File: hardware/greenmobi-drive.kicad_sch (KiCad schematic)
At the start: 32 parts, among them J1 GND, J2 Sensors, J3 UBAT, J4 USB_C_Receptacle_USB2.0_14P, J5 CAN, U1 BMI323, U2 TJA1051T-3

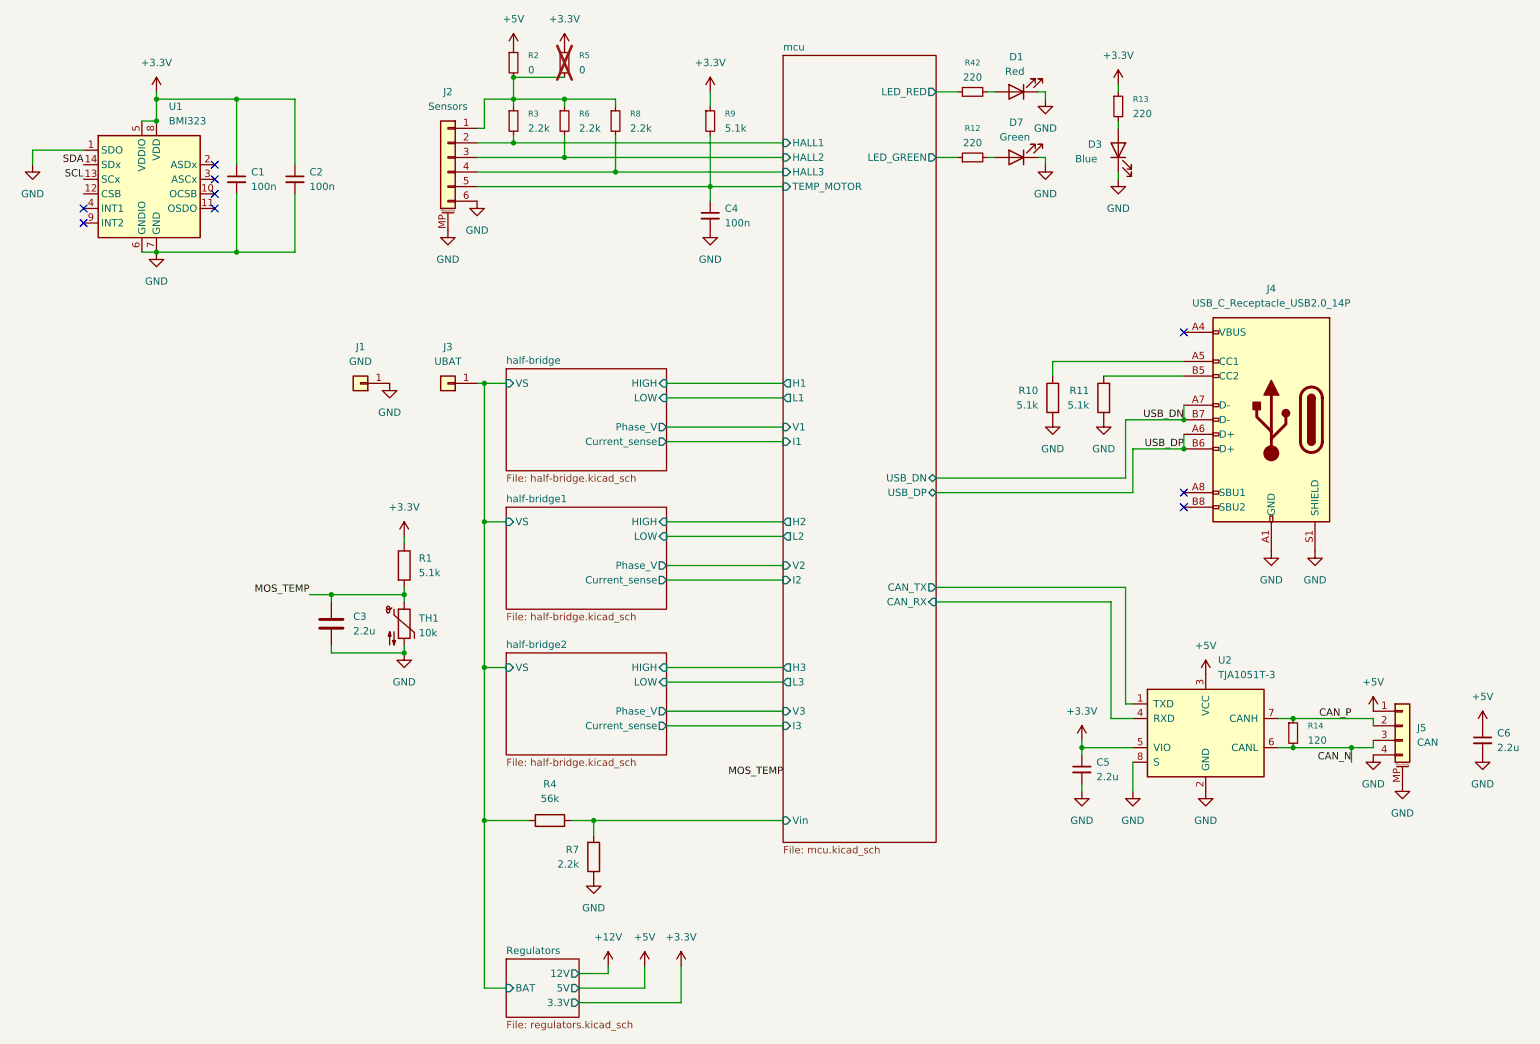
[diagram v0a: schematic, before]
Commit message: Mounting holes alignment
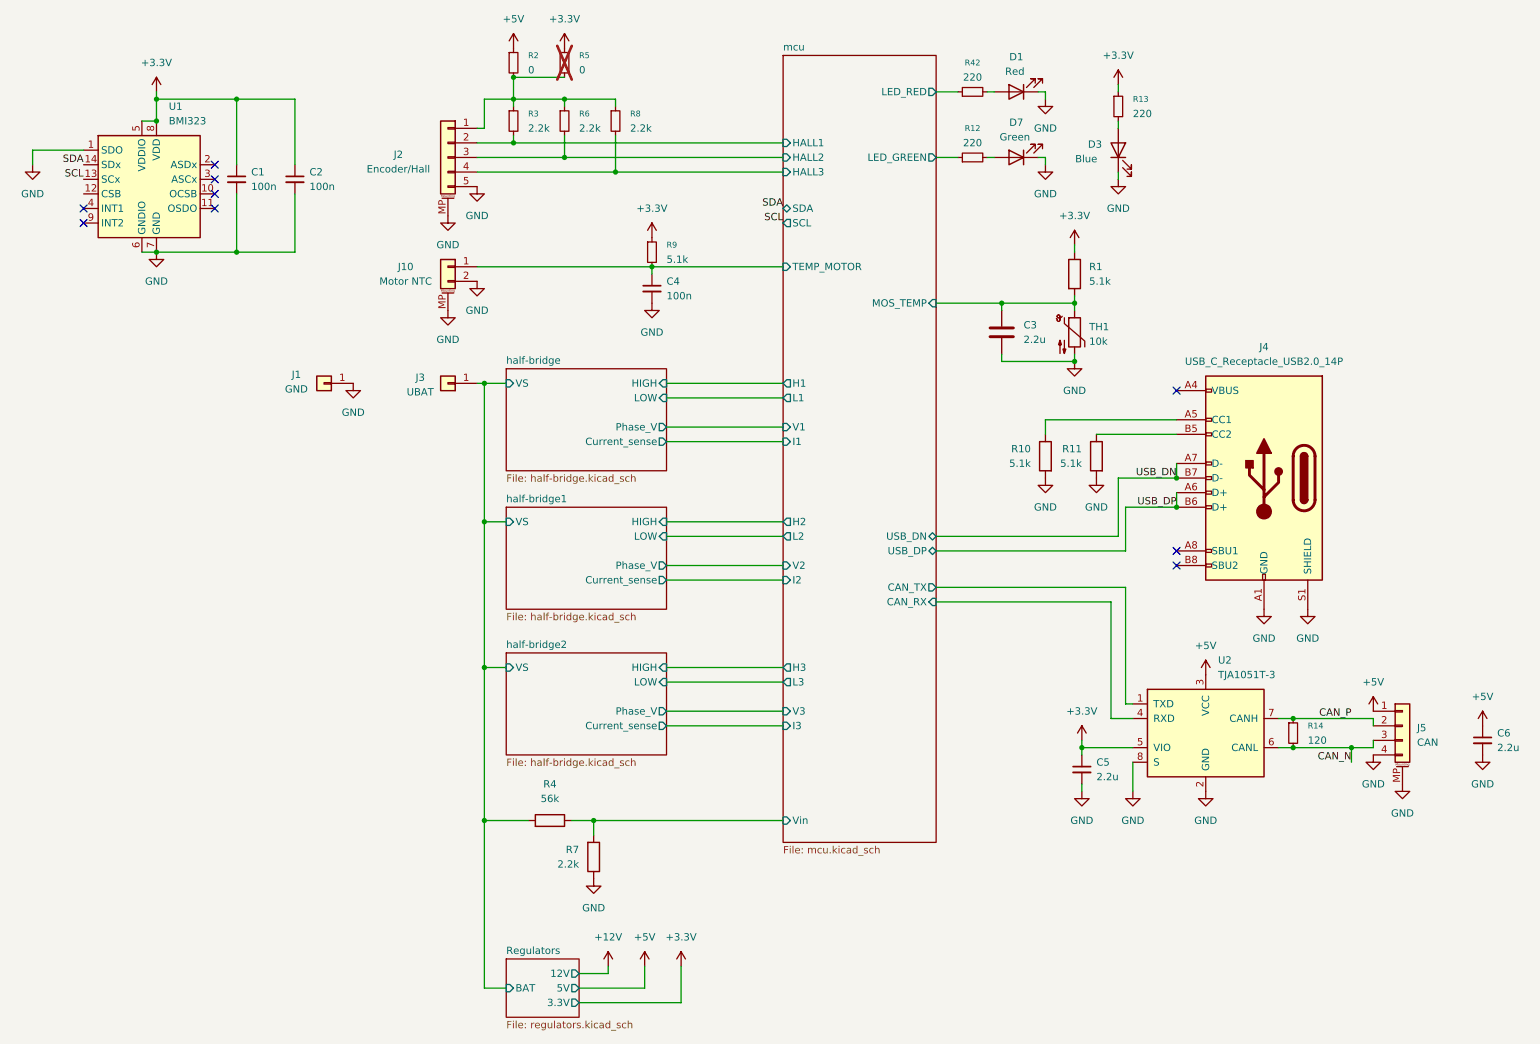
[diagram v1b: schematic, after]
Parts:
- added J10: Motor NTC, Connector_JST:JST_GH_SM02B-GHS-TB_1x02-1MP_P1.25mm_Horizontal, symbol Connector_Generic_MountingPin:Conn_01x02_MountingPin
- J2: value Sensors -> Encoder/Hall; footprint Connector_JST:JST_GH_SM06B-GHS-TB_1x06-1MP_P1.25mm_Horizontal -> Connector_JST:JST_GH_SM05B-GHS-TB_1x05-1MP_P1.25mm_Horizontal; symbol Connector_Generic_MountingPin:Conn_01x06_MountingPin -> Connector_Generic_MountingPin:Conn_01x05_MountingPin
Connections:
- net GND: now also J2.5 (Pin_5), J10.2 (Pin_2), J10.MP (MountPin); no longer J2.6 (Pin_6)
- net mcu/TEMP_MOTOR: now also J10.1 (Pin_1); no longer J2.5 (Pin_5)
- net MOS_TEMP renamed mcu/MOS_TEMP
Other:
- sheet mcu ports: added MOS_TEMP, SCL, SDA; removed none
- moved on the sheet: C3, C4, J1, J4, R1, R10, R11, R9, TH1

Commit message: Capacitors sourced
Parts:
- C1, C2, C4: LCSC (none) -> C77020
- C3, C5, C6: LCSC (none) -> C170151
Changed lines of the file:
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@@
 			)
 		)
-		(property "Sim.Type" ""
-			(at 200.66 69.85 0)
-			(effects
-				(font
-					(size 1.27 1.27)
-				)
-				(hide yes)
-			)
-		)
 		(pin "1"
 		)
@@
 			)
 		)
-		(property "Sim.Type" ""
-			(at 120.65 33.02 0)
-			(effects
-				(font
-					(size 1.27 1.27)
-				)
-				(hide yes)
-			)
-		)
 		(pin "2"
 		)
@@
 			)
 		)
-		(property "Sim.Pins" "1=K 2=A"
-			(at 190.5 39.37 0)
-			(effects
-				(font
-					(size 1.27 1.27)
-				)
-				(hide yes)
-			)
-		)
-		(property "Sim.Type" ""
-			(at 190.5 39.37 0)
-			(effects
-				(font
-					(size 1.27 1.27)
-				)
-				(hide yes)
-			)
-		)
 		(property "LCSC" ""
 			(at 190.5 39.37 90)
@@
 			)
 		)
-		(property "Sim.Type" ""
+		(property "LCSC" "C77020"
 			(at 127 62.23 0)
 			(effects
@@
 			)
 		)
-		(property "Sim.Type" ""
-			(at 111.76 33.02 0)
-			(effects
-				(font
-					(size 1.27 1.27)
-				)
-				(hide yes)
-			)
-		)
 		(pin "2"
 		)
@@
 			)
 		)
-		(property "Sim.Type" ""
+		(property "LCSC" "C170151"
 			(at 201.93 146.05 0)
 			(effects
@@
 			)
 		)
-		(property "Sim.Type" ""
+		(property "LCSC" "C170151"
 			(at 187.96 69.85 0)
 			(effects
@@
 			)
 		)
-		(property "Sim.Type" ""
-			(at 195.58 91.44 0)
-			(effects
-				(font
-					(size 1.27 1.27)
-				)
-				(hide yes)
-			)
-		)
 		(pin "1"
 		)
@@
 			)
 		)
-		(property "Sim.Type" ""
-			(at 69.85 78.74 0)
-			(effects
-				(font
-					(size 1.27 1.27)
-				)
-				(hide yes)
-			)
-		)
 		(pin "1"
 		)
@@
 			)
 		)
-		(property "Sim.Type" ""
-			(at 102.87 22.86 0)
-			(effects
-				(font
-					(size 1.27 1.27)
-				)
-				(hide yes)
-			)
-		)
 		(pin "1"
 		)
@@
 			)
 		)
-		(property "Sim.Type" ""
-			(at 204.47 91.44 0)
-			(effects
-				(font
-					(size 1.27 1.27)
-				)
-				(hide yes)
-			)
-		)
 		(pin "1"
 		)
@@
 			)
 		)
-		(property "Sim.Type" ""
-			(at 238.76 139.7 0)
-			(effects
-				(font
-					(size 1.27 1.27)
-				)
-				(hide yes)
-			)
-		)
 		(pin "2"
 		)
@@
 			)
 		)
+		(property "LCSC" "C77020"
+			(at 54.61 43.18 0)
+			(effects
+				(font
+					(size 1.27 1.27)
+				)
+				(hide yes)
+			)
+		)
 		(pin "2"
 		)
@@
 			)
 		)
-		(property "Sim.Type" ""
-			(at 91.44 78.74 0)
-			(effects
-				(font
-					(size 1.27 1.27)
-				)
-				(hide yes)
-			)
-		)
 		(pin "1"
 		)
@@
 			)
 		)
-		(property "Sim.Type" ""
-			(at 233.68 95.25 0)
-			(effects
-				(font
-					(size 1.27 1.27)
-				)
-				(hide yes)
-			)
-		)
 		(pin "A7"
 		)
@@
 			)
 		)
-		(property "Sim.Type" ""
-			(at 109.22 154.94 90)
-			(effects
-				(font
-					(size 1.27 1.27)
-				)
-				(hide yes)
-			)
-		)
 		(pin "2"
 		)
@@
 			)
 		)
-		(property "Sim.Type" ""
-			(at 116.84 161.29 0)
-			(effects
-				(font
-					(size 1.27 1.27)
-				)
-				(hide yes)
-			)
-		)
 		(pin "2"
 		)
@@
 			)
 		)
+		(property "LCSC" "C77020"
+			(at 64.77 43.18 0)
+			(effects
+				(font
+					(size 1.27 1.27)
+				)
+				(hide yes)
+			)
+		)
 		(pin "2"
 		)
@@
 			)
 		)
-		(property "Sim.Type" ""
-			(at 111.76 22.86 0)
-			(effects
-				(font
-					(size 1.27 1.27)
-				)
-				(hide yes)
-			)
-		)
 		(pin "1"
 		)
@@
 			)
 		)
-		(property "Sim.Type" ""
-			(at 257.81 138.43 0)
-			(effects
-				(font
-					(size 1.27 1.27)
-				)
-				(hide yes)
-			)
-		)
 		(pin "3"
 		)
@@
 			)
 		)
-		(property "Sim.Type" ""
-			(at 223.52 139.7 0)
-			(effects
-				(font
-					(size 1.27 1.27)
-				)
-				(hide yes)
-			)
-		)
 		(pin "6"
 		)
@@
 			)
 		)
-		(property "Sim.Type" ""
-			(at 127 55.88 0)
-			(effects
-				(font
-					(size 1.27 1.27)
-				)
-				(hide yes)
-			)
-		)
 		(pin "2"
 		)
@@
 			)
 		)
-		(property "Sim.Type" ""
-			(at 200.66 59.69 0)
-			(effects
-				(font
-					(size 1.27 1.27)
-				)
-				(hide yes)
-			)
-		)
 		(pin "1"
 		)
@@
 			)
 		)
-		(property "Sim.Pins" "1=K 2=A"
-			(at 190.5 27.94 0)
-			(effects
-				(font
-					(size 1.27 1.27)
-				)
-				(hide yes)
-			)
-		)
-		(property "Sim.Type" ""
-			(at 190.5 27.94 0)
-			(effects
-				(font
-					(size 1.27 1.27)
-				)
-				(hide yes)
-			)
-		)
 		(property "LCSC" ""
 			(at 190.5 27.94 90)
@@
 			)
 		)
-		(property "Sim.Type" ""
-			(at 91.44 39.37 0)
-			(effects
-				(font
-					(size 1.27 1.27)
-				)
-				(hide yes)
-			)
-		)
 		(pin "3"
 		)
@@
 			)
 		)
-		(property "Sim.Pins" "1=K 2=A"
-			(at 208.28 38.1 0)
-			(effects
-				(font
-					(size 1.27 1.27)
-				)
-				(hide yes)
-			)
-		)
-		(property "Sim.Type" ""
-			(at 208.28 38.1 0)
-			(effects
-				(font
-					(size 1.27 1.27)
-				)
-				(hide yes)
-			)
-		)
 		(property "LCSC" ""
 			(at 208.28 38.1 90)
@@
 			)
 		)
-		(property "Sim.Type" ""
+		(property "LCSC" "C170151"
 			(at 271.78 140.97 0)
 			(effects
@@
 			(at 102.87 33.02 0)
 			(effects
-				(font
-					(size 1.27 1.27)
-				)
-				(hide yes)
-			)
-		)
-		(property "Sim.Type" ""
-			(at 102.87 33.02 0)
-			(effects

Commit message: Sourcing complete
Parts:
- D1: LCSC (none) -> C688884
- D3: LCSC (none) -> C779459
- D7: LCSC (none) -> C688883
- J10: LCSC (none) -> C17700380
- J2: LCSC (none) -> C17700383
- J4: LCSC (none) -> C2765186
- J5: LCSC (none) -> C17700382
- R1, R10, R11, R9: LCSC (none) -> C25905
- R12, R13, R42: LCSC (none) -> C2909336
- R14: LCSC (none) -> C25079
- R2, R5: LCSC (none) -> C106231
- R3, R6, R7, R8: LCSC (none) -> C114762
- R4: LCSC (none) -> C17756
- TH1: LCSC (none) -> C77131
- U2: LCSC (none) -> C38695
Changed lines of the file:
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@@
 			)
 		)
+		(property "LCSC" "C77131"
+			(at 200.66 69.85 0)
+			(effects
+				(font
+					(size 1.27 1.27)
+				)
+				(hide yes)
+			)
+		)
 		(pin "1"
 		)
@@
 			)
 		)
+		(property "LCSC" "C2909336"
+			(at 208.28 30.48 0)
+			(effects
+				(font
+					(size 1.27 1.27)
+				)
+				(hide yes)
+			)
+		)
 		(pin "2"
 		)
@@
 			)
 		)
+		(property "LCSC" "C114762"
+			(at 120.65 33.02 0)
+			(effects
+				(font
+					(size 1.27 1.27)
+				)
+				(hide yes)
+			)
+		)
 		(pin "2"
 		)
@@
 			)
 		)
+		(property "LCSC" "C2909336"
+			(at 182.88 39.37 90)
+			(effects
+				(font
+					(size 1.27 1.27)
+				)
+				(hide yes)
+			)
+		)
 		(pin "2"
 		)
@@
 			)
 		)
-		(property "LCSC" ""
+		(property "LCSC" "C688883"
 			(at 190.5 39.37 90)
 			(effects
@@
 			)
 		)
+		(property "LCSC" "C114762"
+			(at 111.76 33.02 0)
+			(effects
+				(font
+					(size 1.27 1.27)
+				)
+				(hide yes)
+			)
+		)
 		(pin "2"
 		)
@@
 			)
 		)
+		(property "LCSC" "C2909336"
+			(at 182.88 27.94 90)
+			(effects
+				(font
+					(size 1.27 1.27)
+				)
+				(hide yes)
+			)
+		)
 		(pin "2"
 		)
@@
 			)
 		)
+		(property "LCSC" "C25905"
+			(at 195.58 91.44 0)
+			(effects
+				(font
+					(size 1.27 1.27)
+				)
+				(hide yes)
+			)
+		)
 		(pin "1"
 		)
@@
 			)
 		)
+		(property "LCSC" "C106231"
+			(at 102.87 22.86 0)
+			(effects
+				(font
+					(size 1.27 1.27)
+				)
+				(hide yes)
+			)
+		)
 		(pin "1"
 		)
@@
 			)
 		)
+		(property "LCSC" "C25905"
+			(at 204.47 91.44 0)
+			(effects
+				(font
+					(size 1.27 1.27)
+				)
+				(hide yes)
+			)
+		)
 		(pin "1"
 		)
@@
 			)
 		)
+		(property "LCSC" "C25079"
+			(at 238.76 139.7 0)
+			(effects
+				(font
+					(size 1.27 1.27)
+				)
+				(hide yes)
+			)
+		)
 		(pin "2"
 		)
@@
 			)
 		)
+		(property "LCSC" "C17700380"
+			(at 91.44 58.42 0)
+			(effects
+				(font
+					(size 1.27 1.27)
+				)
+				(hide yes)
+			)
+		)
 		(pin "1"
 		)
@@
 			)
 		)
+		(property "LCSC" "C2765186"
+			(at 233.68 95.25 0)
+			(effects
+				(font
+					(size 1.27 1.27)
+				)
+				(hide yes)
+			)
+		)
 		(pin "A7"
 		)
@@
 			)
 		)
+		(property "LCSC" "C17756"
+			(at 109.22 154.94 90)
+			(effects
+				(font
+					(size 1.27 1.27)
+				)
+				(hide yes)
+			)
+		)
 		(pin "2"
 		)
@@
 			)
 		)
+		(property "LCSC" "C114762"
+			(at 116.84 161.29 0)
+			(effects
+				(font
+					(size 1.27 1.27)
+				)
+				(hide yes)
+			)
+		)
 		(pin "2"
 		)
@@
 			)
 		)
+		(property "LCSC" "C106231"
+			(at 111.76 22.86 0)
+			(effects
+				(font
+					(size 1.27 1.27)
+				)
+				(hide yes)
+			)
+		)
 		(pin "1"
 		)
@@
 			)
 		)
+		(property "LCSC" "C17700382"
+			(at 257.81 138.43 0)
+			(effects
+				(font
+					(size 1.27 1.27)
+				)
+				(hide yes)
+			)
+		)
 		(pin "3"
 		)
@@
 			)
 		)
+		(property "LCSC" "C38695"
+			(at 223.52 139.7 0)
+			(effects
+				(font
+					(size 1.27 1.27)
+				)
+				(hide yes)
+			)
+		)
 		(pin "6"
 		)
@@
 			)
 		)
+		(property "LCSC" "C25905"
+			(at 127 55.88 0)
+			(effects
+				(font
+					(size 1.27 1.27)
+				)
+				(hide yes)
+			)
+		)
 		(pin "2"
 		)
@@
 			)
 		)
+		(property "LCSC" "C25905"
+			(at 200.66 59.69 0)
+			(effects
+				(font
+					(size 1.27 1.27)
+				)
+				(hide yes)
+			)
+		)
 		(pin "1"
 		)
@@
 			)
 		)
-		(property "LCSC" ""
+		(property "LCSC" "C688884"
 			(at 190.5 27.94 90)
 			(effects
@@
 			)
 		)
+		(property "LCSC" "C17700383"
+			(at 91.44 39.37 0)
+			(effects
+				(font
+					(size 1.27 1.27)
+				)
+				(hide yes)
+			)
+		)
 		(pin "3"
 		)
@@
 			)
 		)
-		(property "LCSC" ""
+		(property "LCSC" "C779459"
 			(at 208.28 38.1 90)
 			(effects
@@
 			(at 102.87 33.02 0)
 			(effects
+				(font
+					(size 1.27 1.27)
+				)
+				(hide yes)
+			)
+		)
+		(property "LCSC" "C114762"
+			(at 102.87 33.02 0)
+			(effects

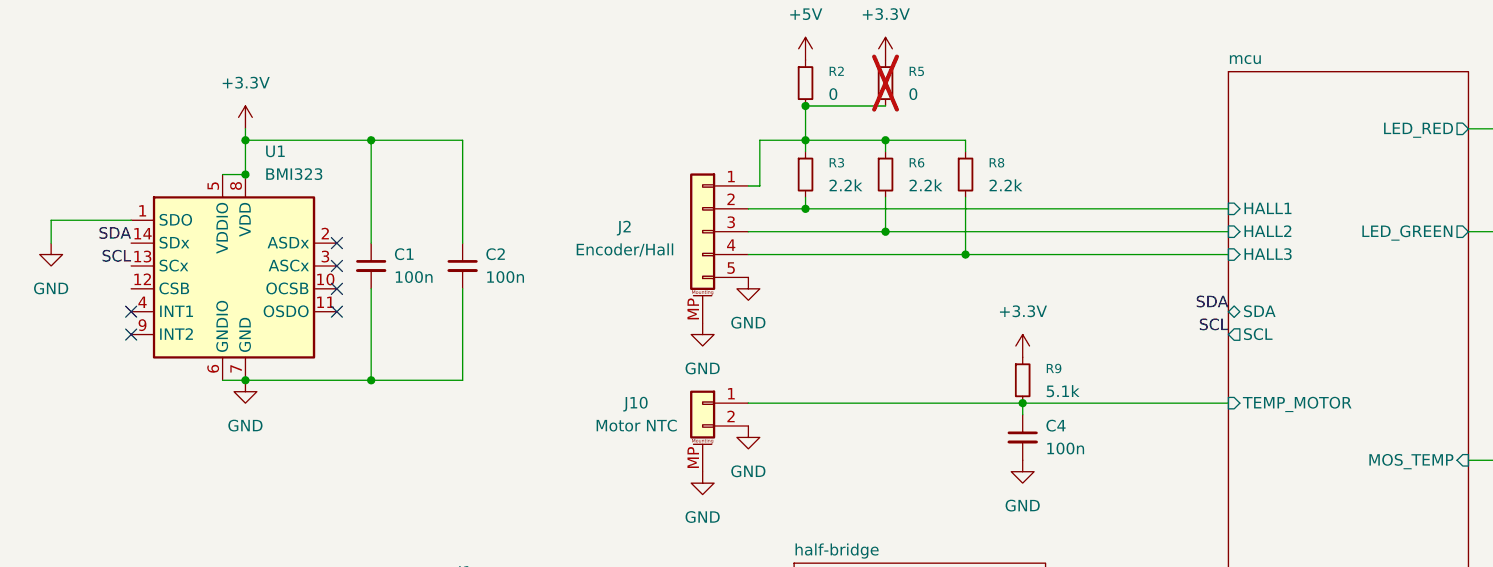
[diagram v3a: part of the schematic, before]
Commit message: Add missing I2C pullups
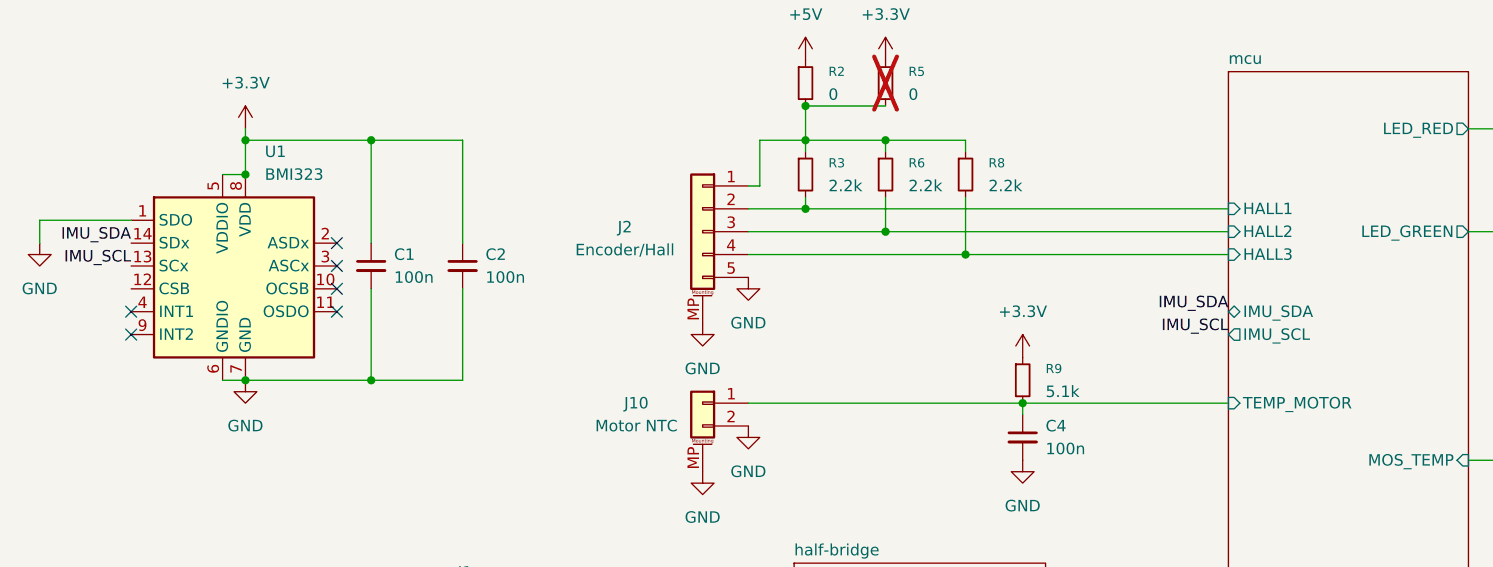
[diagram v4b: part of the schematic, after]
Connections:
- net SCL renamed IMU_SCL
- net SDA renamed IMU_SDA
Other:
- sheet mcu ports: added IMU_SCL, IMU_SDA; removed SCL, SDA
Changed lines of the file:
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@@
 	(wire
 		(pts
-			(xy 19.05 38.1) (xy 27.94 38.1)
+			(xy 17.78 38.1) (xy 27.94 38.1)
 		)
 		(stroke
@@
 	(wire
 		(pts
-			(xy 19.05 38.1) (xy 19.05 40.64)
+			(xy 17.78 38.1) (xy 17.78 40.64)
 		)
 		(stroke
@@
 		)
 	)
-	(label "SDA"
+	(label "IMU_SDA"
 		(at 27.94 40.64 180)
 		(effects
@@
 		)
 	)
-	(label "SCL"
+	(label "IMU_SCL"
 		(at 149.86 50.8 180)
 		(effects
@@
 		)
 	)
-	(label "SDA"
+	(label "IMU_SDA"
 		(at 149.86 48.26 180)
 		(effects
@@
 		)
 	)
-	(label "SCL"
+	(label "IMU_SCL"
 		(at 27.94 43.18 180)
 		(effects
@@
 	(symbol
 		(lib_id "power:GND")
-		(at 19.05 40.64 0)
+		(at 17.78 40.64 0)
 		(unit 1)
 		(exclude_from_sim no)
@@
 		(fields_autoplaced yes)
 		(property "Reference" "#PWR01"
-			(at 19.05 46.99 0)
+			(at 17.78 46.99 0)
 			(effects
 				(font
@@
 		)
 		(property "Value" "GND"
-			(at 19.05 45.72 0)
+			(at 17.78 45.72 0)
 			(effects
 				(font
@@
 		)
 		(property "Footprint" ""
-			(at 19.05 40.64 0)
+			(at 17.78 40.64 0)
 			(effects
 				(font
@@
 		)
 		(property "Datasheet" ""
-			(at 19.05 40.64 0)
+			(at 17.78 40.64 0)
 			(effects
 				(font
@@
 		)
 		(property "Description" "Power symbol creates a global label with name \"GND\" , ground"
-			(at 19.05 40.64 0)
+			(at 17.78 40.64 0)
 			(effects
 				(font
@@
 			)
 		)
-		(pin "SCL" output
+		(pin "IMU_SCL" output
 			(at 149.86 50.8 180)
 			(effects
@@
 			)
 		)
-		(pin "SDA" bidirectional
+		(pin "IMU_SDA" bidirectional
 			(at 149.86 48.26 180)
 			(effects

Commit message: Change power connections to pads instead of holes
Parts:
- J1, J3: footprint MountingHole:MountingHole_5.3mm_M5_DIN965_Pad -> TestPoint:TestPoint_Pad_4.0x4.0mm
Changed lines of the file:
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@@
 			)
 		)
-		(property "Footprint" "MountingHole:MountingHole_5.3mm_M5_DIN965_Pad"
+		(property "Footprint" "TestPoint:TestPoint_Pad_4.0x4.0mm"
 			(at 69.85 78.74 0)
 			(effects
@@
 			)
 		)
-		(property "Footprint" "MountingHole:MountingHole_5.3mm_M5_DIN965_Pad"
+		(property "Footprint" "TestPoint:TestPoint_Pad_4.0x4.0mm"
 			(at 91.44 78.74 0)
 			(effects
